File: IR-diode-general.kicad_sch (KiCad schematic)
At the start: 27 parts, among them J1 PJ-102A, J2 USB4105-GF-A, J3 SM06B-SRSS-TB-LF-SN, J4 SM06B-SRSS-TB-LF-SN, U1 MP2483DQ-LF-P, U2 AZ1117CH-5.0TRG1

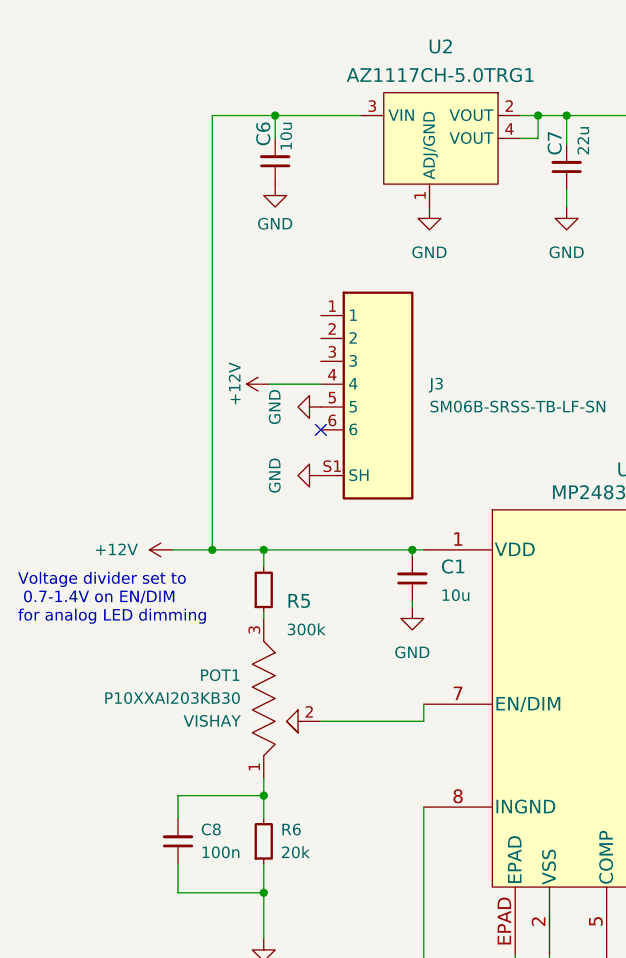
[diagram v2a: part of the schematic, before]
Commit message: Changed the potentiometer to R0141-2-20k
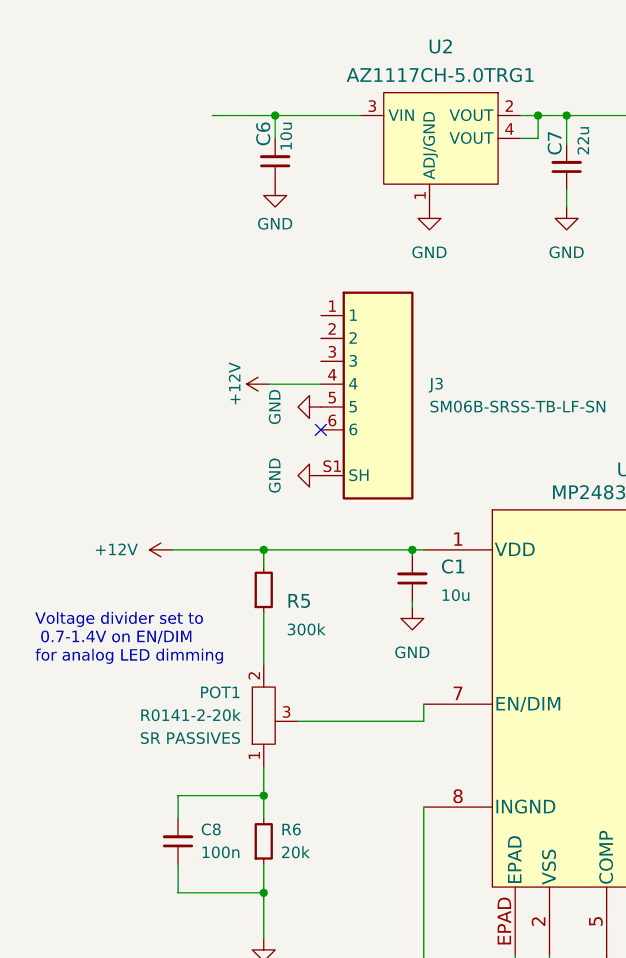
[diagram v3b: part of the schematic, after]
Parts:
- removed POT1: P10XXAI203KB30, antmicro-footprints:P10XHAI203KB30, symbol antmicroRotaryPotentiometersRheostats:P10XXAI203KB30
- added POT1: R0141-2-20k, antmicro-footprints:R0141-2-20k, symbol antmicroRotaryPotentiometersRheostats:R0141-2-20k
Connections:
- net +12V: no longer C6.2, U2.3 (VIN)
- net at C8.2, R6.2: now also POT1.1
- net at U1.7 (EN/DIM): now also POT1.3
- net at R5.1: now also POT1.2
- new net: C6.2, U2.3 (VIN)
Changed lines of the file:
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@@
   (junction (at 235.585 121.285) (diameter 0) (color 0 0 0 0)
-  )
-  (junction (at 121.285 121.285) (diameter 0) (color 0 0 0 0)
   )
   (junction (at 245.11 118.11) (diameter 0) (color 0 0 0 0)
@@
     (stroke (width 0) (type default) (color 0 0 0 0))
   )
-  (wire (pts (xy 127 128.27) (xy 127 128.905))
+  (wire (pts (xy 127 128.27) (xy 127 133.985))
     (stroke (width 0) (type default) (color 0 0 0 0))
   )
@@
     (stroke (width 0) (type default) (color 0 0 0 0))
   )
-  (wire (pts (xy 133.35 140.335) (xy 144.78 140.335))
+  (wire (pts (xy 130.81 140.335) (xy 144.78 140.335))
     (stroke (width 0) (type default) (color 0 0 0 0))
   )
@@
     (stroke (width 0) (type default) (color 0 0 0 0))
   )
-  (wire (pts (xy 116.84 121.285) (xy 121.285 121.285))
+  (wire (pts (xy 116.84 121.285) (xy 127 121.285))
     (stroke (width 0) (type default) (color 0 0 0 0))
   )
@@
     (stroke (width 0) (type default) (color 0 0 0 0))
   )
-  (wire (pts (xy 121.285 121.285) (xy 127 121.285))
-    (stroke (width 0) (type default) (color 0 0 0 0))
-  )
   (wire (pts (xy 189.865 138.43) (xy 203.2 138.43))
     (stroke (width 0) (type default) (color 0 0 0 0))
@@
     (stroke (width 0) (type default) (color 0 0 0 0))
   )
-  (wire (pts (xy 121.285 73.025) (xy 121.285 121.285))
-    (stroke (width 0) (type default) (color 0 0 0 0))
-  )
   (wire (pts (xy 253.365 145.415) (xy 253.365 150.495))
     (stroke (width 0) (type default) (color 0 0 0 0))
@@
     (stroke (width 0) (type default) (color 0 0 0 0))
   )
-  (wire (pts (xy 127 148.59) (xy 127 146.685))
+  (wire (pts (xy 127 145.415) (xy 127 148.59))
     (stroke (width 0) (type default) (color 0 0 0 0))
   )
@@
   )
   (text "Voltage divider set to\n 0.7-1.4V on EN/DIM\nfor analog LED dimming"
-    (at 99.695 129.54 0)
+    (at 101.6 133.985 0)
     (effects (font (size 1.27 1.27)) (justify left bottom))
   )
@@
       (effects (font (size 1.27 1.27)) (justify right) hide)
     )
-  )
-  (symbol (lib_id "antmicroRotaryPotentiometersRheostats:P10XXAI203KB30") (at 127 149.225 90) (unit 1)
-    (in_bom yes) (on_board yes) (fields_autoplaced)
-    (property "Reference" "POT1" (id 0) (at 124.46 135.2549 90)
-      (effects (font (size 1.27 1.27)) (justify left))
-    )
-    (property "Value" "P10XXAI203KB30" (id 1) (at 124.46 137.7949 90)
-      (effects (font (size 1.27 1.27)) (justify left))
-    )
-    (property "Footprint" "antmicro-footprints:P10XHAI203KB30" (id 2) (at 135.89 147.955 0)
-      (effects (font (size 1.27 1.27)) hide)
-    )
-    (property "Datasheet" "https://www.farnell.com/datasheets/2243933.pdf" (id 3) (at 138.176 147.701 0)
-      (effects (font (size 1.27 1.27)) hide)
-    )
-    (property "MPN" "P10XXAI203KB30" (id 4) (at 144.78 149.225 0)
-      (effects (font (size 1.27 1.27)) hide)
-    )
-    (property "Manufacturer" "VISHAY" (id 5) (at 124.46 140.3349 90)
-      (effects (font (size 1.27 1.27)) (justify left))
-    )
-    (property "Copyright" "Copyright (c) 2023 Antmicro" (id 6) (at 139.954 148.717 0)
-      (effects (font (size 1.27 1.27)) hide)
-    )
-    (property "License" "Apache-2.0 License" (id 7) (at 141.986 148.209 0)
-      (effects (font (size 1.27 1.27)) hide)
-    )
-    (pin "1")
-    (pin "2")
-    (pin "3")
   )
   (symbol (lib_id "power:GND") (at 222.885 148.59 0) (unit 1)
@@
     (pin "5")
   )
+  (symbol (lib_id "antmicroRotaryPotentiometersRheostats:R0141-2-20k") (at 127 145.415 90) (unit 1)
+    (in_bom yes) (on_board yes) (fields_autoplaced)
+    (property "Reference" "POT1" (id 0) (at 124.46 137.1599 90)
+      (effects (font (size 1.27 1.27)) (justify left))
+    )
+    (property "Value" "R0141-2-20k" (id 1) (at 124.46 139.6999 90)
+      (effects (font (size 1.27 1.27)) (justify left))
+    )
+    (property "Footprint" "antmicro-footprints:R0141-2-20k" (id 2) (at 134.62 114.935 0)
+      (effects (font (size 1.27 1.27)) hide)
+    )
+    (property "Datasheet" "https://www.tme.eu/Document/48eb4fb11c5e0c9b1cd467745dfbcb98/R0141-2.pdf" (id 3) (at 139.7 133.985 0)
+      (effects (font (size 1.27 1.27)) hide)
+    )
+    (property "MPN" "R0141-2-20k" (id 4) (at 137.16 125.095 0)
+      (effects (font (size 1.27 1.27)) hide)
+    )
+    (property "Manufacturer" "SR PASSIVES" (id 5) (at 124.46 142.2399 90)
+      (effects (font (size 1.27 1.27)) (justify left))
+    )
+    (property "Copyright" "Copyright (c) 2023 Antmicro" (id 6) (at 142.24 135.255 0)
+      (effects (font (size 1.27 1.27)) hide)
+    )
+    (property "License" "Apache-2.0" (id 7) (at 144.78 128.905 0)
+      (effects (font (size 1.27 1.27)) hide)
+    )
+    (pin "1")
+    (pin "2")
+    (pin "3")
+  )
   (symbol (lib_id "antmicroCapacitors0402:C_100n_0402") (at 189.865 133.35 90) (unit 1)
     (in_bom yes) (on_board yes) (fields_autoplaced)
@@
       (reference "L1") (unit 1) (value "SRP2512A-4R7M") (footprint "antmicro-footprints:SRP2512A-1R0M")
     )
-    (path "/0430b26c-d49a-4185-95d4-7a8f67c12206"
-      (reference "POT1") (unit 1) (value "P10XXAI203KB30") (footprint "antmicro-footprints:P10XHAI203KB30")
+    (path "/d86f9cb8-27af-476c-9aee-602255382645"
+      (reference "POT1") (unit 1) (value "R0141-2-20k") (footprint "antmicro-footprints:R0141-2-20k")
     )
     (path "/e3e4e911-7d88-487f-8c9e-68bd8e697b19"

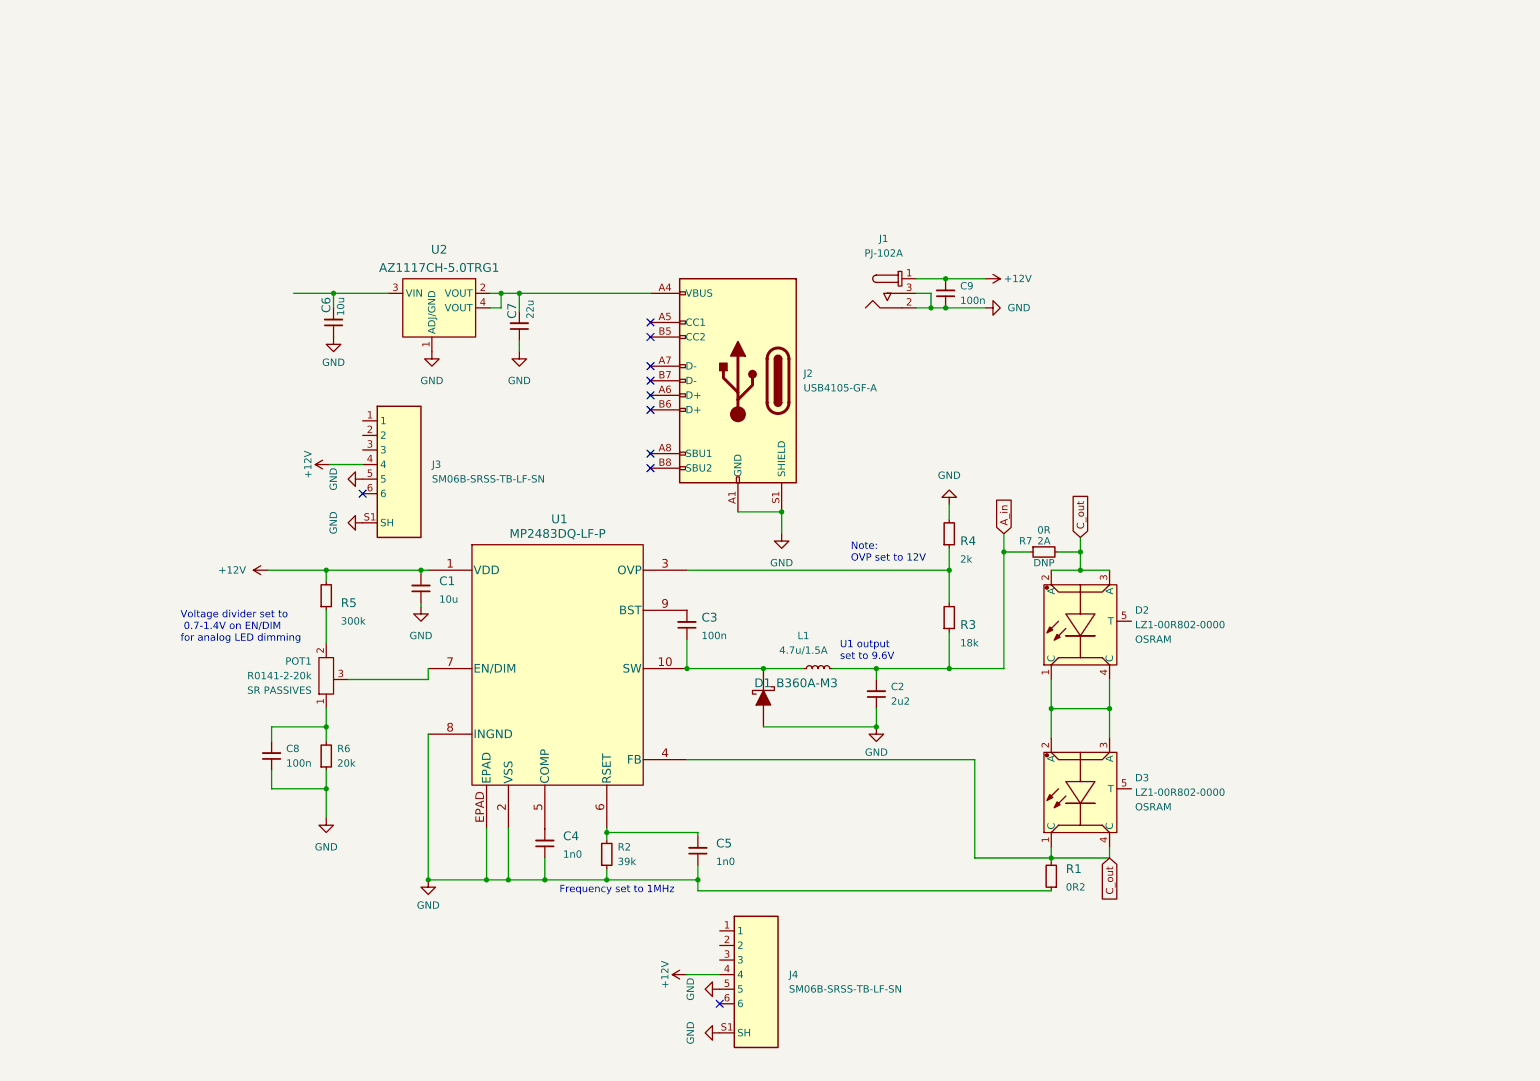
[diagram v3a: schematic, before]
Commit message: Changed the 12V-5V converter
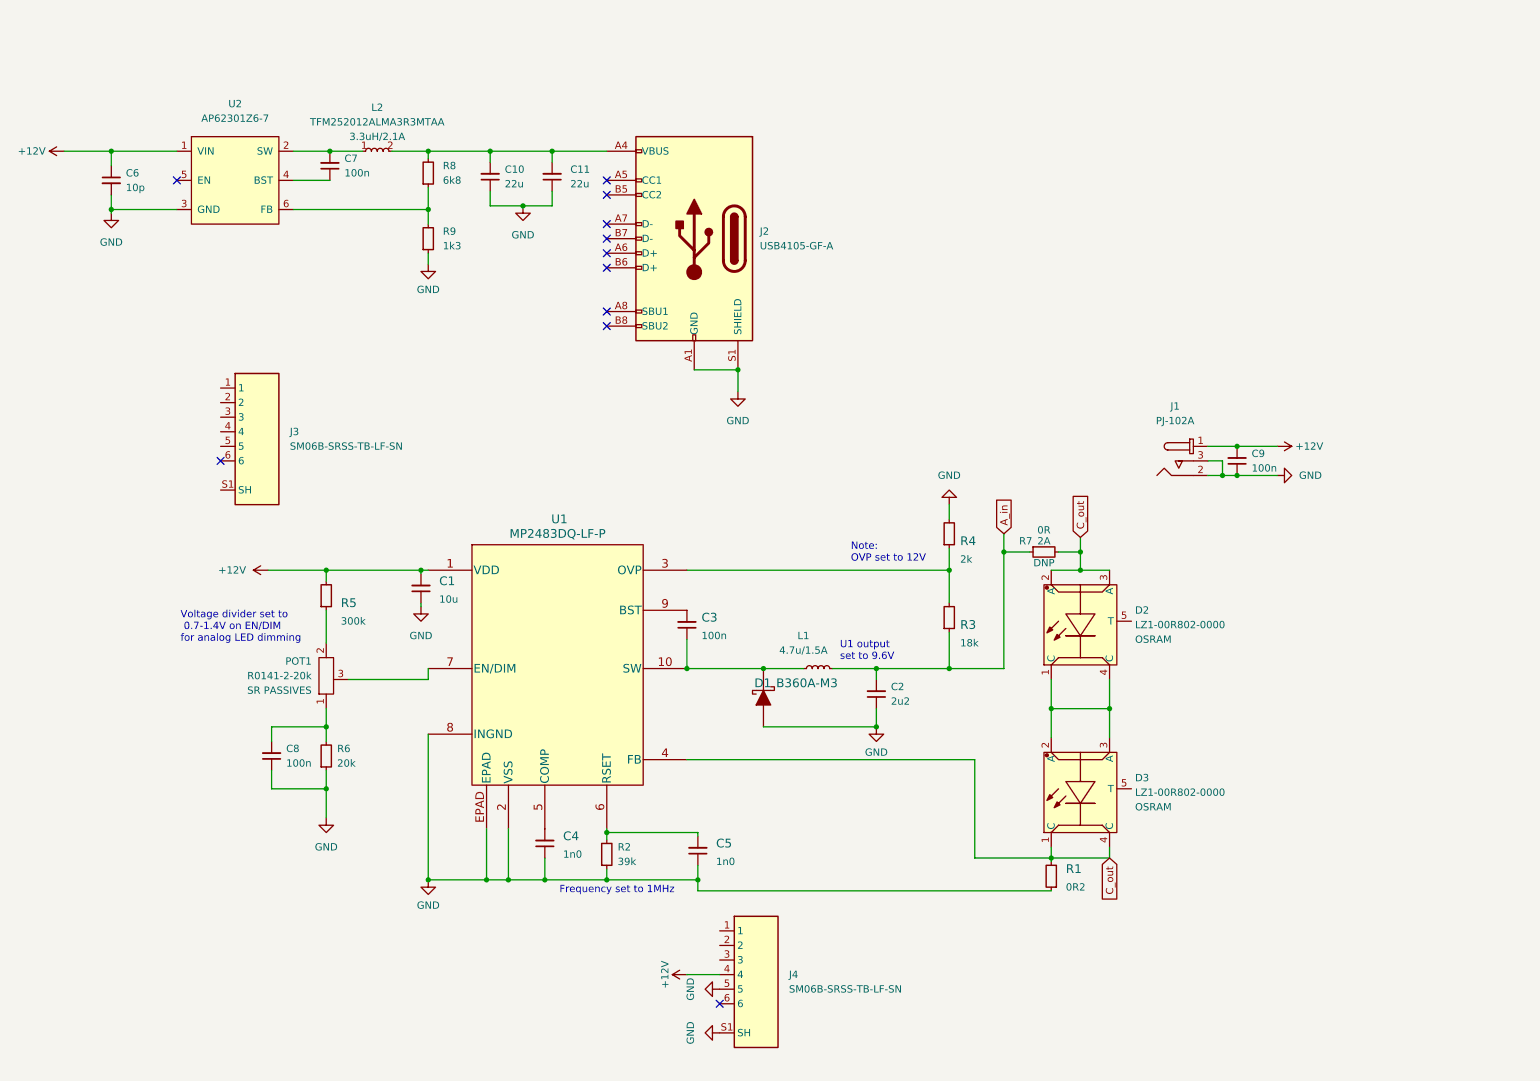
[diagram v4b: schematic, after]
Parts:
- removed C6: C_10u_0805, antmicro-footprints:0805-cap, symbol antmicroCapacitorsmisc:C_10u_0805
- removed C7: C_22u_0402, antmicro-footprints:C_0402_1005Metric, symbol antmicroCapacitors0402:C_22u_0402
- removed U2: AZ1117CH-5.0TRG1, antmicro-footprints:SOT-223, symbol antmicroPMICVoltageRegulatorsLinear:AZ1117CH-5.0TRG1
- added C10, C11: C_22u_0603, antmicro-footprints:C_0603_1608Metric, symbol antmicroCapacitors0603:C_22u_0603
- added C6: C_10p_0402, antmicro-footprints:C_0402_1005Metric, symbol antmicroCapacitors0402:C_10p_0402
- added C7: C_100n_0402, antmicro-footprints:C_0402_1005Metric, symbol antmicroCapacitors0402:C_100n_0402
- added L2: TFM252012ALMA3R3MTAA, antmicro-footprints:L_1008_2520Metric, symbol antmicroFixedInductors:TFM252012ALMA3R3MTAA
- added R8: R_6k8_0402, antmicro-footprints:0402-res, symbol antmicroResistors0402:R_6k8_0402
- added R9: R_1k3_0402, antmicro-footprints:R_0402_1005Metric, symbol antmicroResistors0402:R_1k3_0402
- added U2: AP62301Z6-7, antmicro-footprints:SOT-563, symbol antmicroDCDCConverters:AP62301Z6-7
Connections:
- net +12V: now also C6.1, U2.1 (VIN); no longer J3.4
- net GND: now also C10.1, C11.1, C6.2, R9.1, U2.3 (GND); no longer J3.5, J3.S1 (SH), J3.S2 (SH)
- net at J2.A4 (VBUS), J2.A9 (VBUS), J2.B4 (VBUS)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: now also C10.2, C11.2, L2.2, R8.2
- new net: C7.2, L2.1, U2.2 (SW)
- new net: C7.1, U2.4 (BST)
- new net: R8.1, R9.2, U2.6 (FB)
- new net: J3.S1 (SH), J3.S2 (SH)
- no-connect marks 10 -> 11
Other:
- moved on the sheet: C9, J1, J2, J3

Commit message: Layout and schematic updates
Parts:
- removed J1: PJ-102A, antmicro-footprints:Barrel_Jack_5.5mmODx2.1mmID_PJ-102A, symbol antmicroBarrelPowerConnectors:PJ-102A
- removed J3, J4: SM06B-SRSS-TB-LF-SN, antmicro-footprints:JST_SM06B-SRSS-TB-LF-SN, symbol antmicroRectangularConnectorsHeadersMalePins:SM06B-SRSS-TB-LF-SN
- removed R1: R_0R2_1206, antmicro-footprints:1206-res, symbol antmicroResistorsmisc:R_0R2_1206
- added J1: BarrelJack_3167288, antmicro-footprints:BarrelJack_3167288_Horizontal, symbol antmicroBarrelAudioConnectors:BarrelJack_3167288
- added R2: R_0R2_1206, antmicro-footprints:1206-res, symbol antmicroResistorsmisc:R_0R2_1206
- added R? (x2): R_0R_1206, antmicro-footprints:R_1206_3216Metric, symbol antmicroResistorsmisc:R_0R_1206
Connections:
- net +12V: now also J1.1
- net A_in: now also D2.2 (A), D2.3 (A), R7.2; no longer C2.2, L1.2, R3.1, R7.1
- net C_out: now also R?.1, R?.1; no longer D2.2 (A), D2.3 (A), D3.1 (C), D3.4 (C), R7.2, U1.4 (FB)
- net GND: now also J1.2, J1.3, R2.1
- new net: D3.1 (C), D3.4 (C), R2.2, R?.2, U1.4 (FB)
- new net: C2.2, L1.2, R3.1, R7.1, R?.2
- no-connect marks 11 -> 9
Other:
- note added: "MASTER"
- note added: "MASTER DP"
- note added: "SLAVE DP"
- note added: "VFB = 0.8025V"
